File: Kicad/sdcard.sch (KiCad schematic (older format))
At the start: 4 parts, among them J301 SD_Card

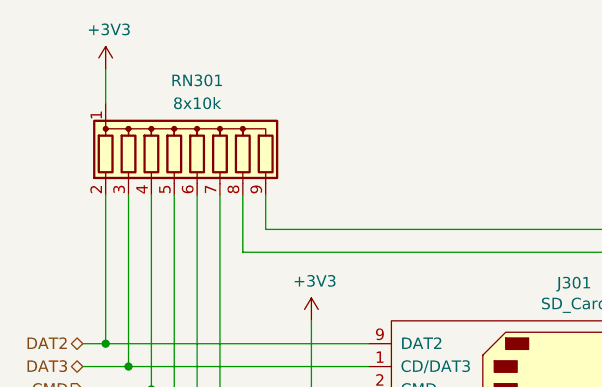
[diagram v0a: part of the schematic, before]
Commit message: Update component values.
Tolerance and Voltage are set to the minimum acceptable. The selected
parts can be better, where a better part is cheaper or has
better availability.

Also dropped R2R DAC tolerance to 1% - 0.5% was overkill. The output
resistor had the wrong value too, which is fixed.
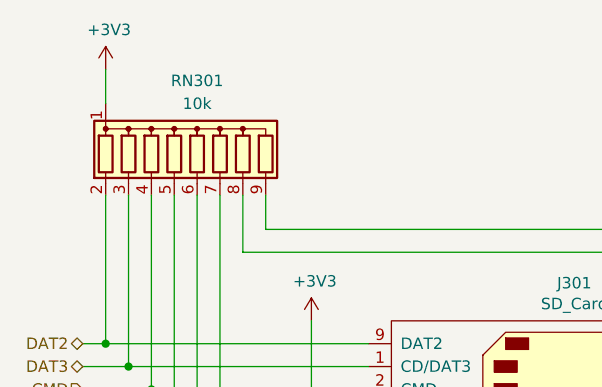
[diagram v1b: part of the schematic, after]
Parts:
- C301: Tolerance (none) -> X5R; Voltage (none) -> 16V
- C302: Tolerance (none) -> X5R; Voltage (none) -> 50V
- RN301: value 8x10k -> 10k; Tolerance (none) -> 2%
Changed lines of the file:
@@
 F 8 "581-145638009211859+" H 5950 3750 50  0001 C CNN "Mouser"
 F 9 "~" H 5950 3750 50  0001 C CNN "LCSC Part#"
+F 10 "~" H 5950 3750 50  0001 C CNN "Tolerance"
+F 11 "~" H 5950 3750 50  0001 C CNN "Voltage"
 	1    5950 3750
 	1    0    0    -1
@@
 F 3 "~" H 8250 3750 50  0001 C CNN
 F 4 "0" H 8250 3750 50  0001 C CNN "DNP"
-F 5 "" H 8250 3750 50  0001 C CNN "Digikey"
+F 5 "~" H 8250 3750 50  0001 C CNN "Digikey"
 F 6 "CPL-CAP-X5R-0805-10UF-16V" H 8250 3750 50  0001 C CNN "MPN"
 F 7 "CPL" H 8250 3750 50  0001 C CNN "Manufacturer"
 F 8 "C15850" H 8250 3750 50  0001 C CNN "LCSC Part#"
+F 9 "X5R" H 8250 3750 50  0001 C CNN "Tolerance"
+F 10 "16V" H 8250 3750 50  0001 C CNN "Voltage"
+F 11 "~" H 8250 3750 50  0001 C CNN "Mouser"
 	1    8250 3750
 	1    0    0    -1
@@
 F 3 "~" H 8800 3750 50  0001 C CNN
 F 4 "0" H 8800 3750 50  0001 C CNN "DNP"
-F 5 "" H 8800 3750 50  0001 C CNN "Digikey"
+F 5 "~" H 8800 3750 50  0001 C CNN "Digikey"
 F 6 "CPL-CAP-X7R-0805-100NF-50V" H 8800 3750 50  0001 C CNN "MPN"
 F 7 "CPL" H 8800 3750 50  0001 C CNN "Manufacturer"
-F 8 "" H 8800 3750 50  0001 C CNN "Mouser"
+F 8 "~" H 8800 3750 50  0001 C CNN "Mouser"
 F 9 "C49678" H 8800 3750 50  0001 C CNN "LCSC Part#"
+F 10 "X5R" H 8800 3750 50  0001 C CNN "Tolerance"
+F 11 "50V" H 8800 3750 50  0001 C CNN "Voltage"
 	1    8800 3750
 	1    0    0    -1
@@
 P 4300 2500
 F 0 "RN301" H 4300 2800 50  0000 C CNN
-F 1 "8x10k" H 4300 2700 50  0000 C CNN
+F 1 "10k" H 4300 2700 50  0000 C CNN
 F 2 "Resistor_THT:R_Array_SIP9" V 4675 2500 50  0001 C CNN
 F 3 "http://www.vishay.com/docs/31509/csc.pdf" H 4300 2500 50  0001 C CNN
@@
 F 8 "652-4609X-1LF-10K" H 4300 2500 50  0001 C CNN "Mouser"
 F 9 "~" H 4300 2500 50  0001 C CNN "LCSC Part#"
+F 10 "2%" H 4300 2500 50  0001 C CNN "Tolerance"
+F 11 "~" H 4300 2500 50  0001 C CNN "Voltage"
 	1    4300 2500
 	1    0    0    -1

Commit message: Drop capacitor voltage ratings where possible.
Audio circuit is 1V RMS, so 6.3V is fine.
Use 10V for 3.3V circuits.
Use 16V for 5.0V circuits.
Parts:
- C301: Voltage 16V -> 10V
- C302: Voltage 50V -> 10V
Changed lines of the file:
@@
 F 8 "C15850" H 8250 3750 50  0001 C CNN "LCSC Part#"
 F 9 "X5R" H 8250 3750 50  0001 C CNN "Tolerance"
-F 10 "16V" H 8250 3750 50  0001 C CNN "Voltage"
+F 10 "10V" H 8250 3750 50  0001 C CNN "Voltage"
 F 11 "~" H 8250 3750 50  0001 C CNN "Mouser"
 	1    8250 3750
@@
 F 9 "C49678" H 8800 3750 50  0001 C CNN "LCSC Part#"
 F 10 "X5R" H 8800 3750 50  0001 C CNN "Tolerance"
-F 11 "50V" H 8800 3750 50  0001 C CNN "Voltage"
+F 11 "10V" H 8800 3750 50  0001 C CNN "Voltage"
 	1    8800 3750
 	1    0    0    -1

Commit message: Added expansion header.
Involved rerouting quite a few things.
Also added through-hole switches for power/reset.
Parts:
- renumbered C301 to C201, C302 to C202, J301 to J201, RN301 to RN201
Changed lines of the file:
@@
 $EndDescr
 $Comp
-L Connector:SD_Card J301
+L Connector:SD_Card J201
 U 1 1 5FE7BB6E
 P 5950 3750
-F 0 "J301" H 5950 4415 50  0000 C CNN
+F 0 "J201" H 5950 4415 50  0000 C CNN
 F 1 "SD_Card" H 5950 4324 50  0000 C CNN
 F 2 "Connector_Card:SD_Kyocera_145638009211859+" H 5950 3750 50  0001 C CNN
@@
 DAT1
 $Comp
-L power:+3V3 #PWR0302
+L power:+3V3 #PWR0202
 U 1 1 5FE7CAA7
 P 4800 3250
-F 0 "#PWR0302" H 4800 3100 50  0001 C CNN
+F 0 "#PWR0202" H 4800 3100 50  0001 C CNN
 F 1 "+3V3" H 4815 3423 50  0000 C CNN
 F 2 "" H 4800 3250 50  0001 C CNN
@@
 	4800 3750 4800 3250
 $Comp
-L power:GND #PWR0303
+L power:GND #PWR0203
 U 1 1 5FE7D47D
 P 4900 4250
-F 0 "#PWR0303" H 4900 4000 50  0001 C CNN
+F 0 "#PWR0203" H 4900 4000 50  0001 C CNN
 F 1 "GND" H 4905 4077 50  0000 C CNN
 F 2 "" H 4900 4250 50  0001 C CNN
@@
 	4400 4150 3800 4150
 $Comp
-L power:+3V3 #PWR0301
+L power:+3V3 #PWR0201
 U 1 1 5FE8424F
 P 3900 2150
-F 0 "#PWR0301" H 3900 2000 50  0001 C CNN
+F 0 "#PWR0201" H 3900 2000 50  0001 C CNN
 F 1 "+3V3" H 3915 2323 50  0000 C CNN
 F 2 "" H 3900 2150 50  0001 C CNN
@@
 	3900 2150 3900 2300
 $Comp
-L power:+3V3 #PWR0305
+L power:+3V3 #PWR0205
 U 1 1 5FE84AEC
 P 8250 3500
-F 0 "#PWR0305" H 8250 3350 50  0001 C CNN
+F 0 "#PWR0205" H 8250 3350 50  0001 C CNN
 F 1 "+3V3" H 8265 3673 50  0000 C CNN
 F 2 "" H 8250 3500 50  0001 C CNN
@@
 $EndComp
 $Comp
-L power:GND #PWR0306
+L power:GND #PWR0206
 U 1 1 5FE84E43
 P 8250 4000
-F 0 "#PWR0306" H 8250 3750 50  0001 C CNN
+F 0 "#PWR0206" H 8250 3750 50  0001 C CNN
 F 1 "GND" H 8255 3827 50  0000 C CNN
 F 2 "" H 8250 4000 50  0001 C CNN
@@
 $EndComp
 $Comp
-L Device:CP C301
+L Device:CP C201
 U 1 1 5FE85358
 P 8250 3750
-F 0 "C301" H 8368 3796 50  0000 L CNN
+F 0 "C201" H 8368 3796 50  0000 L CNN
 F 1 "10uF" H 8368 3705 50  0000 L CNN
 F 2 "Capacitor_SMD:C_0805_2012Metric_Pad1.18x1.45mm_HandSolder" H 8288 3600 50  0001 C CNN
@@
 $EndComp
 $Comp
-L Device:C C302
+L Device:C C202
 U 1 1 5FE86138
 P 8800 3750
-F 0 "C302" H 8915 3796 50  0000 L CNN
+F 0 "C202" H 8915 3796 50  0000 L CNN
 F 1 "100nF" H 8915 3705 50  0000 L CNN
 F 2 "Capacitor_SMD:C_0805_2012Metric_Pad1.18x1.45mm_HandSolder" H 8838 3600 50  0001 C CNN
@@
 Connection ~ 8250 3950
 $Comp
-L power:GND #PWR0304
+L power:GND #PWR0204
 U 1 1 5FE89E21
 P 6950 4250
-F 0 "#PWR0304" H 6950 4000 50  0001 C CNN
+F 0 "#PWR0204" H 6950 4000 50  0001 C CNN
 F 1 "GND" H 6955 4077 50  0000 C CNN
 F 2 "" H 6950 4250 50  0001 C CNN
@@
 ~WRITE_PROTECT
 $Comp
-L Device:R_Network08 RN301
+L Device:R_Network08 RN201
 U 1 1 5FE7DE1F
 P 4300 2500
-F 0 "RN301" H 4300 2800 50  0000 C CNN
+F 0 "RN201" H 4300 2800 50  0000 C CNN
 F 1 "10k" H 4300 2700 50  0000 C CNN
 F 2 "Resistor_THT:R_Array_SIP9" V 4675 2500 50  0001 C CNN
